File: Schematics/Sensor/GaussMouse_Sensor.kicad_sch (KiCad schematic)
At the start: 47 parts, among them J1 Prog, J2 Conn_01x02, J3 OledDisplay, J4 Conn_01x09, SW1 SW_Push_45deg, SW2 SW_Push_45deg, SW3 SW_Push_45deg, U1 BNO085, U2 CH32V003F4P6, Y1 Crystal_Small

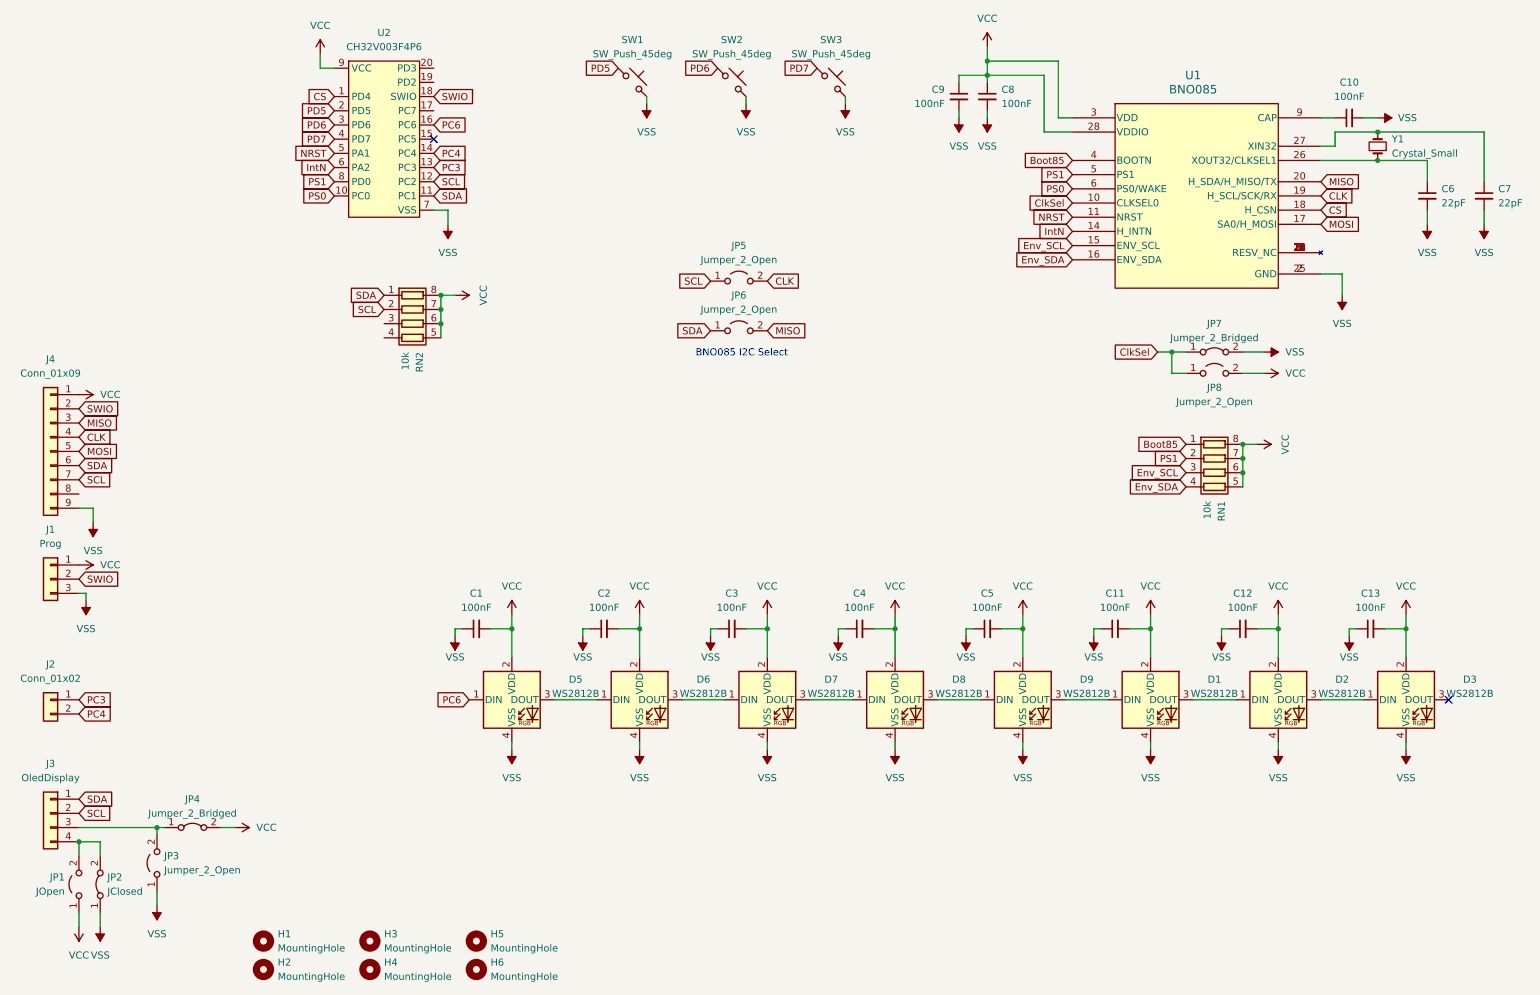
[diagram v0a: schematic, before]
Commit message: Commit for backup. Short on sensor board so I'm going to redo it
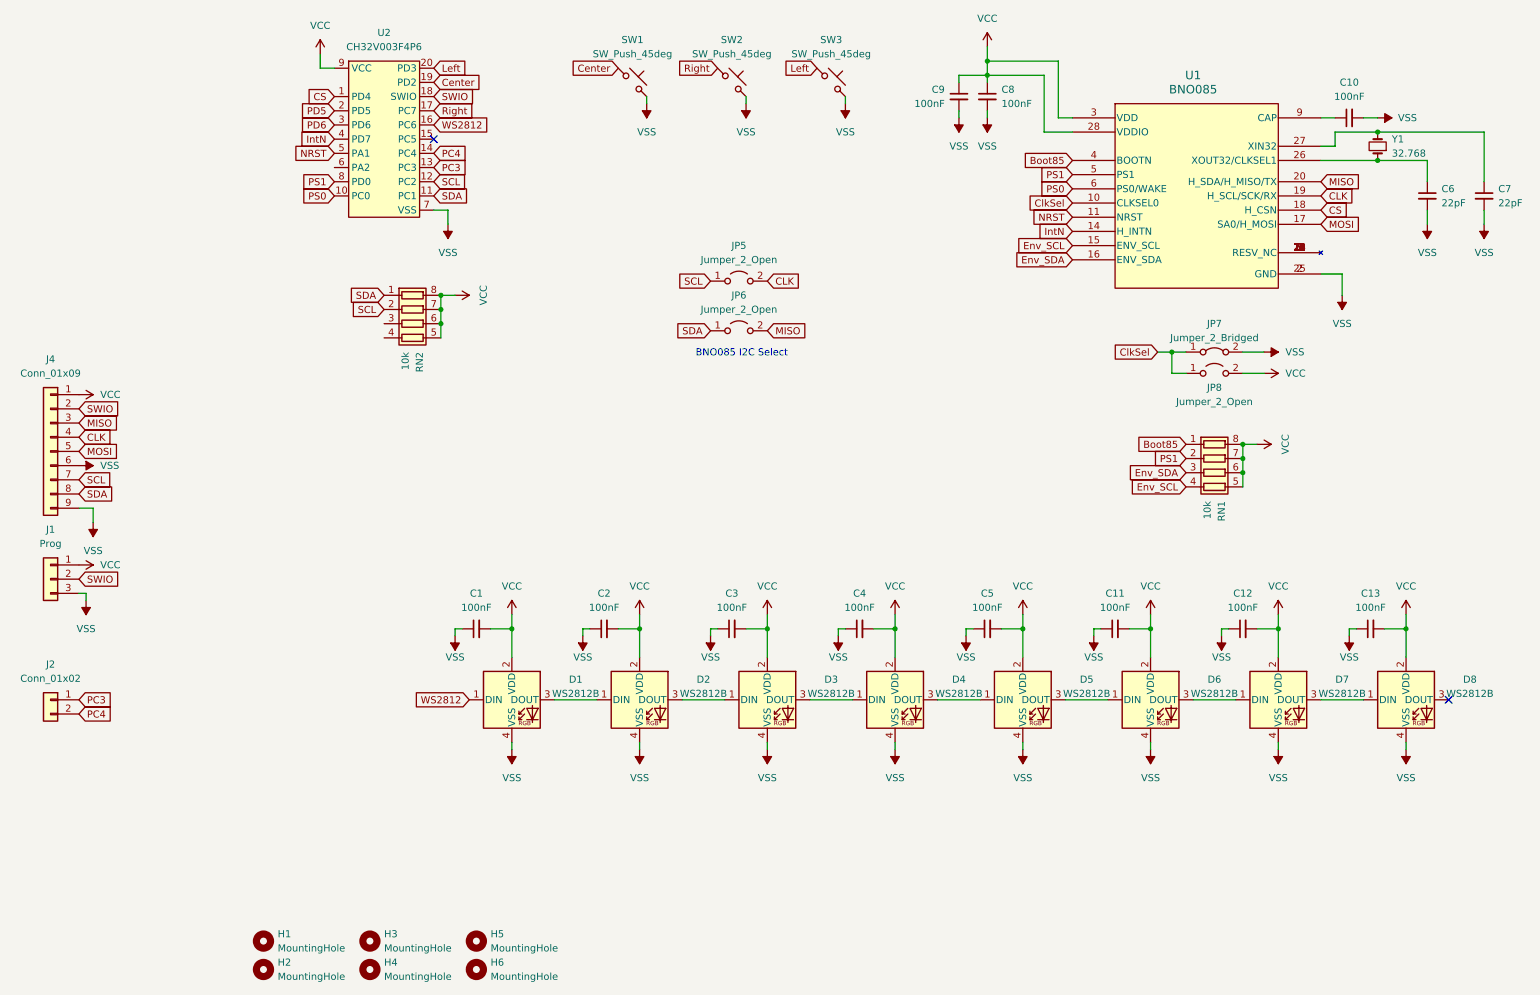
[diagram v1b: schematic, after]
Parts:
- removed J3: OledDisplay, Connector_PinHeader_2.54mm:PinHeader_1x04_P2.54mm_Vertical, symbol Connector_Generic:Conn_01x04
- removed JP1: JOpen, Jumper:SolderJumper-2_P1.3mm_Open_TrianglePad1.0x1.5mm, symbol Jumper:Jumper_2_Open
- removed JP2: JClosed, Jumper:SolderJumper-2_P1.3mm_Bridged_Pad1.0x1.5mm, symbol Jumper:Jumper_2_Bridged
- removed JP3: Jumper_2_Open, Jumper:SolderJumper-2_P1.3mm_Open_TrianglePad1.0x1.5mm, symbol Jumper:Jumper_2_Open
- removed JP4: Jumper_2_Bridged, Jumper:SolderJumper-2_P1.3mm_Bridged_Pad1.0x1.5mm, symbol Jumper:Jumper_2_Bridged
- Y1: value Crystal_Small -> 32.768
- renumbered D5 to D1, D6 to D2, D7 to D3, D8 to D4, D9 to D5, D1 to D6, D2 to D7, D3 to D8
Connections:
- net Env_SCL: now also RN1.4 (R4.1); no longer RN1.3 (R3.1)
- net Env_SDA: now also RN1.3 (R3.1); no longer RN1.4 (R4.1)
- net IntN: now also U2.4 (PD7); no longer U2.6 (PA2)
- net PD5: no longer SW1.1
- net PD6: no longer SW2.1
- net SDA: now also J4.8 (Pin_8); no longer J4.6 (Pin_6)
- net VSS: now also J4.6 (Pin_6)
- net Right: now reaches U2.17 (PC7)
- net Right: now also SW2.1
- net Center: now reaches U2.19 (PD2)
- net Center: now also SW1.1
- net Left: now reaches U2.20 (PD3)
- net Left: now also SW3.1
- net PC6 renamed WS2812
- removed net PD7: SW3.1, U2.4 (PD7)
